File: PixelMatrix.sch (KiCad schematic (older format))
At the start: 75 parts

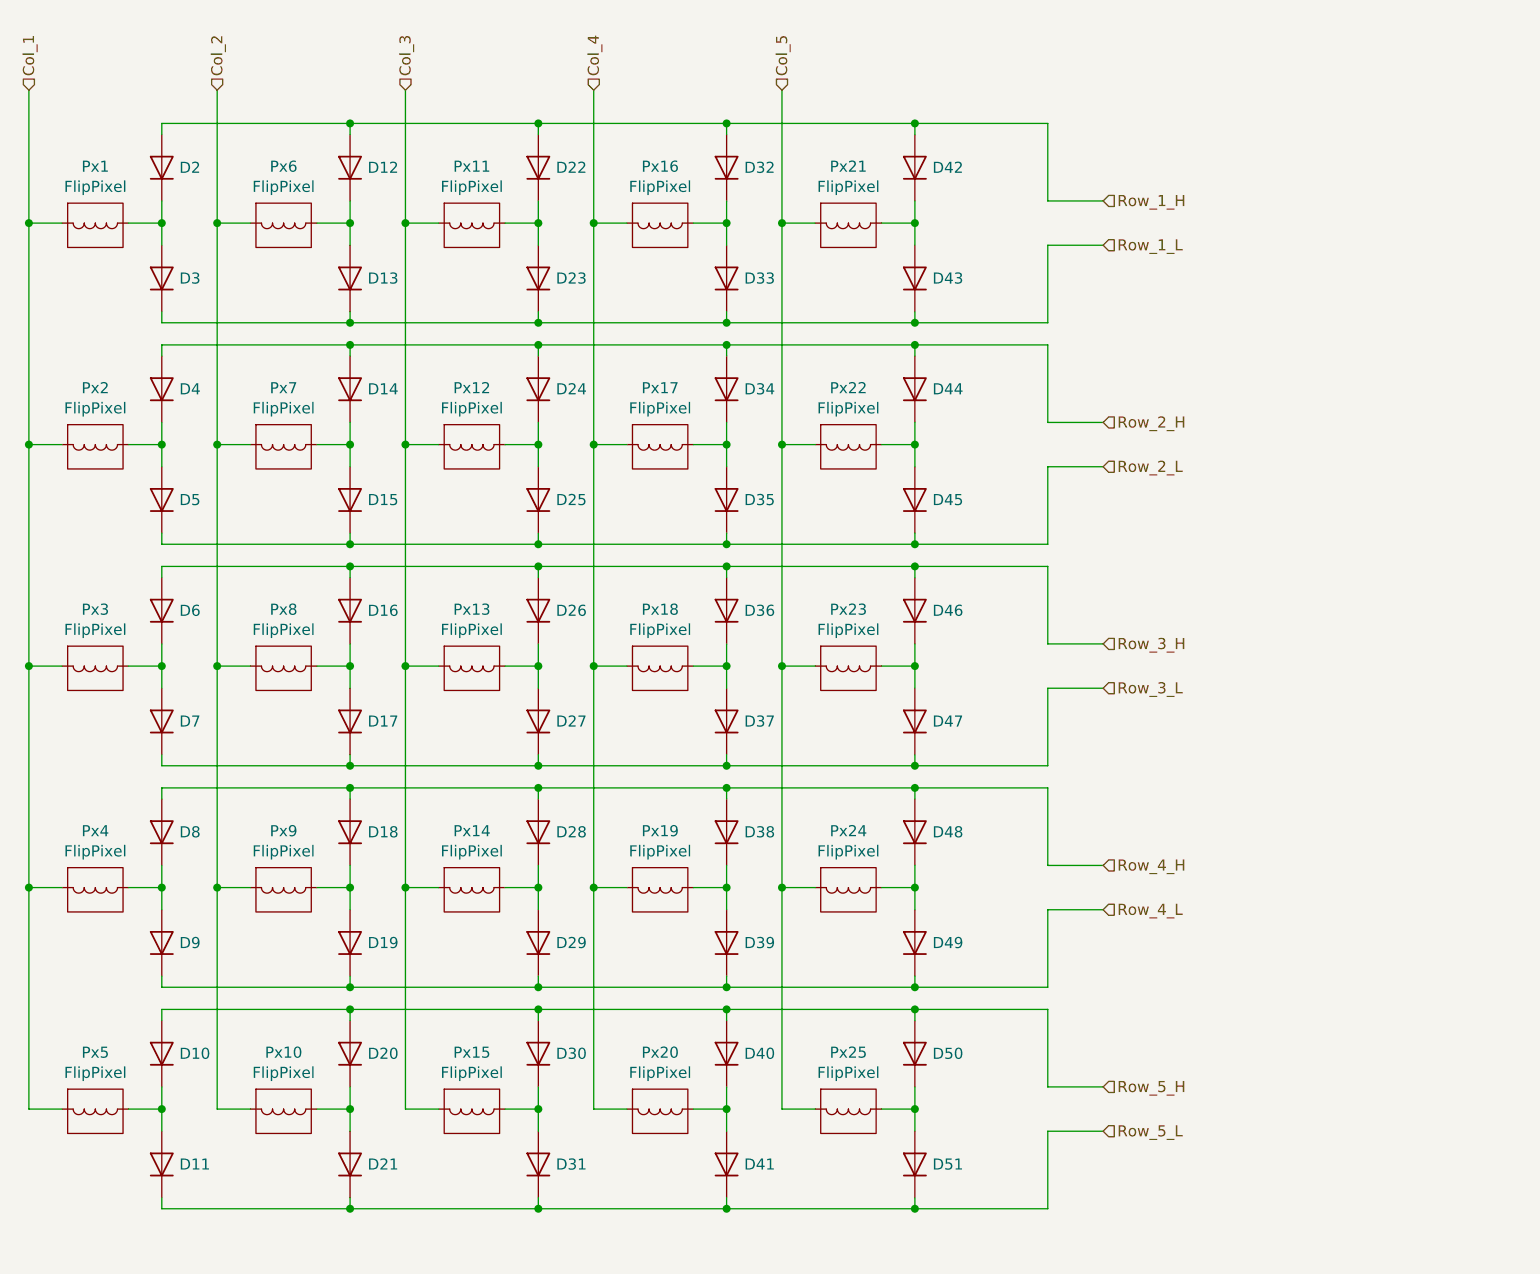
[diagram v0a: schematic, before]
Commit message: Added charge pump for gate driving, MicroController, and Power Connector
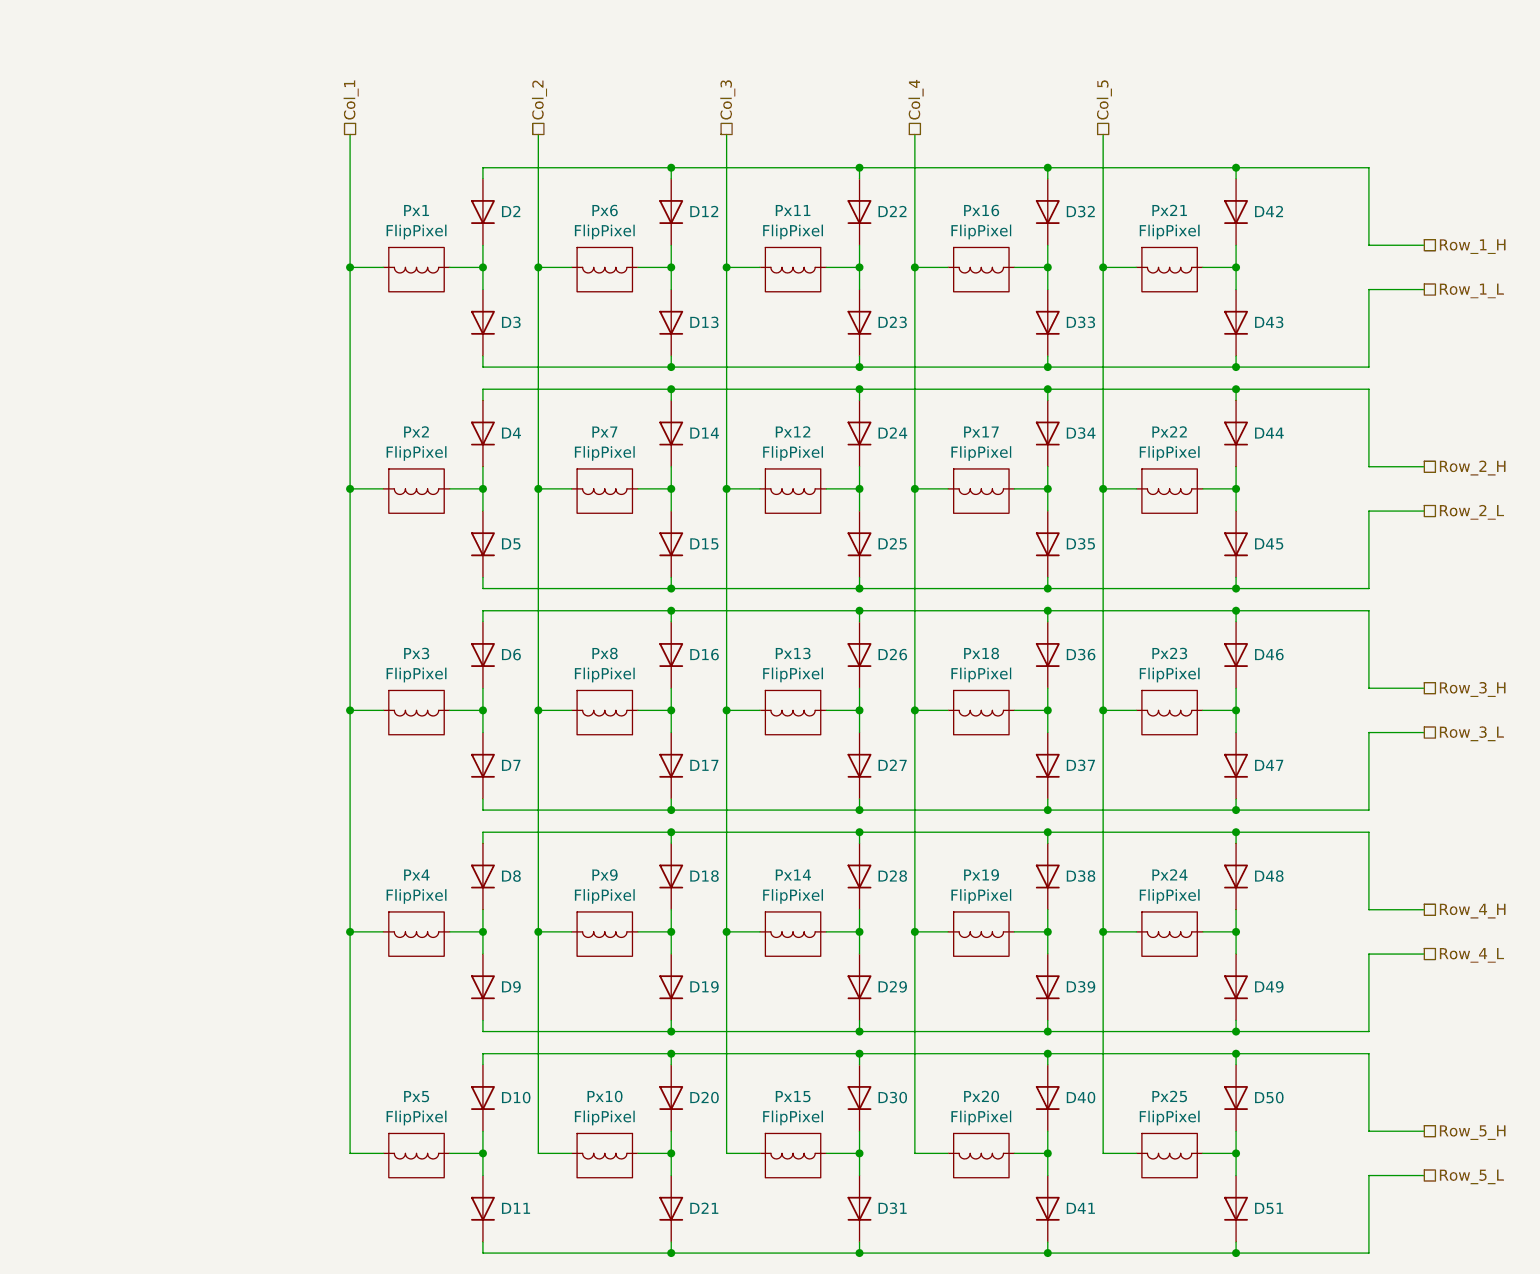
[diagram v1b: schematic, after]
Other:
- moved on the sheet: D10, D11, D12, D13, D14, D15, D16, D17, D18, D19, D2, D20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

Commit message: Started work on layout
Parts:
- Px1, Px10, Px11, Px12, Px13, Px14, Px15, Px16, Px17, Px18, Px19, Px2, Px20, Px21, Px22, Px23, Px24, Px25, Px3, Px4, Px5, Px6, Px7, Px8, Px9: footprint (none) -> Custom-Footprints:Flip-Pixel
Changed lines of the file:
@@
 encoding utf-8
 Sheet 2 12
-Title ""
-Date ""
+Title "Flip Pixel Board"
+Date "2020-06-20"
 Rev ""
 Comp ""
@@
 F 0 "Px20" H 5850 6355 50  0000 C CNN
 F 1 "FlipPixel" H 5850 6264 50  0000 C CNN
-F 2 "" H 5725 6375 50  0001 C CNN
+F 2 "Custom-Footprints:Flip-Pixel" H 5725 6375 50  0001 C CNN
 F 3 "" H 5725 6375 50  0001 C CNN
 	1    5850 6100
@@
 F 0 "Px15" H 5000 6355 50  0000 C CNN
 F 1 "FlipPixel" H 5000 6264 50  0000 C CNN
-F 2 "" H 4875 6375 50  0001 C CNN
+F 2 "Custom-Footprints:Flip-Pixel" H 4875 6375 50  0001 C CNN
 F 3 "" H 4875 6375 50  0001 C CNN
 	1    5000 6100
@@
 F 0 "Px10" H 4150 6355 50  0000 C CNN
 F 1 "FlipPixel" H 4150 6264 50  0000 C CNN
-F 2 "" H 4025 6375 50  0001 C CNN
+F 2 "Custom-Footprints:Flip-Pixel" H 4025 6375 50  0001 C CNN
 F 3 "" H 4025 6375 50  0001 C CNN
 	1    4150 6100
@@
 F 0 "Px5" H 3300 6355 50  0000 C CNN
 F 1 "FlipPixel" H 3300 6264 50  0000 C CNN
-F 2 "" H 3175 6375 50  0001 C CNN
+F 2 "Custom-Footprints:Flip-Pixel" H 3175 6375 50  0001 C CNN
 F 3 "" H 3175 6375 50  0001 C CNN
 	1    3300 6100
@@
 F 0 "Px25" H 6700 6355 50  0000 C CNN
 F 1 "FlipPixel" H 6700 6264 50  0000 C CNN
-F 2 "" H 6575 6375 50  0001 C CNN
+F 2 "Custom-Footprints:Flip-Pixel" H 6575 6375 50  0001 C CNN
 F 3 "" H 6575 6375 50  0001 C CNN
 	1    6700 6100
@@
 F 0 "Px19" H 5850 5355 50  0000 C CNN
 F 1 "FlipPixel" H 5850 5264 50  0000 C CNN
-F 2 "" H 5725 5375 50  0001 C CNN
+F 2 "Custom-Footprints:Flip-Pixel" H 5725 5375 50  0001 C CNN
 F 3 "" H 5725 5375 50  0001 C CNN
 	1    5850 5100
@@
 F 0 "Px14" H 5000 5355 50  0000 C CNN
 F 1 "FlipPixel" H 5000 5264 50  0000 C CNN
-F 2 "" H 4875 5375 50  0001 C CNN
+F 2 "Custom-Footprints:Flip-Pixel" H 4875 5375 50  0001 C CNN
 F 3 "" H 4875 5375 50  0001 C CNN
 	1    5000 5100
@@
 F 0 "Px9" H 4150 5355 50  0000 C CNN
 F 1 "FlipPixel" H 4150 5264 50  0000 C CNN
-F 2 "" H 4025 5375 50  0001 C CNN
+F 2 "Custom-Footprints:Flip-Pixel" H 4025 5375 50  0001 C CNN
 F 3 "" H 4025 5375 50  0001 C CNN
 	1    4150 5100
@@
 F 0 "Px4" H 3300 5355 50  0000 C CNN
 F 1 "FlipPixel" H 3300 5264 50  0000 C CNN
-F 2 "" H 3175 5375 50  0001 C CNN
+F 2 "Custom-Footprints:Flip-Pixel" H 3175 5375 50  0001 C CNN
 F 3 "" H 3175 5375 50  0001 C CNN
 	1    3300 5100
@@
 F 0 "Px24" H 6700 5355 50  0000 C CNN
 F 1 "FlipPixel" H 6700 5264 50  0000 C CNN
-F 2 "" H 6575 5375 50  0001 C CNN
+F 2 "Custom-Footprints:Flip-Pixel" H 6575 5375 50  0001 C CNN
 F 3 "" H 6575 5375 50  0001 C CNN
 	1    6700 5100
@@
 F 0 "Px18" H 5850 4355 50  0000 C CNN
 F 1 "FlipPixel" H 5850 4264 50  0000 C CNN
-F 2 "" H 5725 4375 50  0001 C CNN
+F 2 "Custom-Footprints:Flip-Pixel" H 5725 4375 50  0001 C CNN
 F 3 "" H 5725 4375 50  0001 C CNN
 	1    5850 4100
@@
 F 0 "Px13" H 5000 4355 50  0000 C CNN
 F 1 "FlipPixel" H 5000 4264 50  0000 C CNN
-F 2 "" H 4875 4375 50  0001 C CNN
+F 2 "Custom-Footprints:Flip-Pixel" H 4875 4375 50  0001 C CNN
 F 3 "" H 4875 4375 50  0001 C CNN
 	1    5000 4100
@@
 F 0 "Px8" H 4150 4355 50  0000 C CNN
 F 1 "FlipPixel" H 4150 4264 50  0000 C CNN
-F 2 "" H 4025 4375 50  0001 C CNN
+F 2 "Custom-Footprints:Flip-Pixel" H 4025 4375 50  0001 C CNN
 F 3 "" H 4025 4375 50  0001 C CNN
 	1    4150 4100
@@
 F 0 "Px3" H 3300 4355 50  0000 C CNN
 F 1 "FlipPixel" H 3300 4264 50  0000 C CNN
-F 2 "" H 3175 4375 50  0001 C CNN
+F 2 "Custom-Footprints:Flip-Pixel" H 3175 4375 50  0001 C CNN
 F 3 "" H 3175 4375 50  0001 C CNN
 	1    3300 4100
@@
 F 0 "Px23" H 6700 4355 50  0000 C CNN
 F 1 "FlipPixel" H 6700 4264 50  0000 C CNN
-F 2 "" H 6575 4375 50  0001 C CNN
+F 2 "Custom-Footprints:Flip-Pixel" H 6575 4375 50  0001 C CNN
 F 3 "" H 6575 4375 50  0001 C CNN
 	1    6700 4100
@@
 F 0 "Px17" H 5850 3355 50  0000 C CNN
 F 1 "FlipPixel" H 5850 3264 50  0000 C CNN
-F 2 "" H 5725 3375 50  0001 C CNN
+F 2 "Custom-Footprints:Flip-Pixel" H 5725 3375 50  0001 C CNN
 F 3 "" H 5725 3375 50  0001 C CNN
 	1    5850 3100
@@
 F 0 "Px12" H 5000 3355 50  0000 C CNN
 F 1 "FlipPixel" H 5000 3264 50  0000 C CNN
-F 2 "" H 4875 3375 50  0001 C CNN
+F 2 "Custom-Footprints:Flip-Pixel" H 4875 3375 50  0001 C CNN
 F 3 "" H 4875 3375 50  0001 C CNN
 	1    5000 3100
@@
 F 0 "Px7" H 4150 3355 50  0000 C CNN
 F 1 "FlipPixel" H 4150 3264 50  0000 C CNN
-F 2 "" H 4025 3375 50  0001 C CNN
+F 2 "Custom-Footprints:Flip-Pixel" H 4025 3375 50  0001 C CNN
 F 3 "" H 4025 3375 50  0001 C CNN
 	1    4150 3100
@@
 F 0 "Px2" H 3300 3355 50  0000 C CNN
 F 1 "FlipPixel" H 3300 3264 50  0000 C CNN
-F 2 "" H 3175 3375 50  0001 C CNN
+F 2 "Custom-Footprints:Flip-Pixel" H 3175 3375 50  0001 C CNN
 F 3 "" H 3175 3375 50  0001 C CNN
 	1    3300 3100
@@
 F 0 "Px22" H 6700 3355 50  0000 C CNN
 F 1 "FlipPixel" H 6700 3264 50  0000 C CNN
-F 2 "" H 6575 3375 50  0001 C CNN
+F 2 "Custom-Footprints:Flip-Pixel" H 6575 3375 50  0001 C CNN
 F 3 "" H 6575 3375 50  0001 C CNN
 	1    6700 3100
@@
 F 0 "Px16" H 5850 2355 50  0000 C CNN
 F 1 "FlipPixel" H 5850 2264 50  0000 C CNN
-F 2 "" H 5725 2375 50  0001 C CNN
+F 2 "Custom-Footprints:Flip-Pixel" H 5725 2375 50  0001 C CNN
 F 3 "" H 5725 2375 50  0001 C CNN
 	1    5850 2100
@@
 Wire Wire Line
 	4000 2100 3850 2100
-Wire Wire Line
-	4850 2100 4700 2100
 Wire Wire Line
 	5300 2000 5300 2100
@@
 F 0 "Px11" H 5000 2355 50  0000 C CNN
 F 1 "FlipPixel" H 5000 2264 50  0000 C CNN
-F 2 "" H 4875 2375 50  0001 C CNN
+F 2 "Custom-Footprints:Flip-Pixel" H 4875 2375 50  0001 C CNN
 F 3 "" H 4875 2375 50  0001 C CNN
 	1    5000 2100
@@
 F 0 "Px6" H 4150 2355 50  0000 C CNN
 F 1 "FlipPixel" H 4150 2264 50  0000 C CNN
-F 2 "" H 4025 2375 50  0001 C CNN
+F 2 "Custom-Footprints:Flip-Pixel" H 4025 2375 50  0001 C CNN
 F 3 "" H 4025 2375 50  0001 C CNN
 	1    4150 2100
@@
 F 0 "Px1" H 3300 2355 50  0000 C CNN
 F 1 "FlipPixel" H 3300 2264 50  0000 C CNN
-F 2 "" H 3175 2375 50  0001 C CNN
+F 2 "Custom-Footprints:Flip-Pixel" H 3175 2375 50  0001 C CNN
 F 3 "" H 3175 2375 50  0001 C CNN
 	1    3300 2100
@@
 F 0 "Px21" H 6700 2355 50  0000 C CNN
 F 1 "FlipPixel" H 6700 2264 50  0000 C CNN
-F 2 "" H 6575 2375 50  0001 C CNN
+F 2 "Custom-Footprints:Flip-Pixel" H 6575 2375 50  0001 C CNN
 F 3 "" H 6575 2375 50  0001 C CNN
 	1    6700 2100
@@
 Wire Wire Line
 	4700 6100 4700 5100
-Connection ~ 4700 2100
 Connection ~ 4700 3100
-Wire Wire Line
-	4700 3100 4700 2100
 Connection ~ 4700 4100
 Wire Wire Line
@@
 Wire Wire Line
 	5550 2100 5550 1500
-Wire Wire Line
-	4700 2100 4700 1500
 Wire Wire Line
 	3850 2100 3850 1500
@@
 Text HLabel 3000 1500 1    50   UnSpc ~ 0
 Col_1
+Wire Wire Line
+	4700 2100 4700 1500
+Wire Wire Line
+	4700 3100 4700 2100
+Connection ~ 4700 2100
+Wire Wire Line
+	4850 2100 4700 2100
 $EndSCHEMATC
